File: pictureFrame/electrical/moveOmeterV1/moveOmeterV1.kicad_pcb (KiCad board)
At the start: 2 copper layers, 11 parts, among them U1 SEN0623

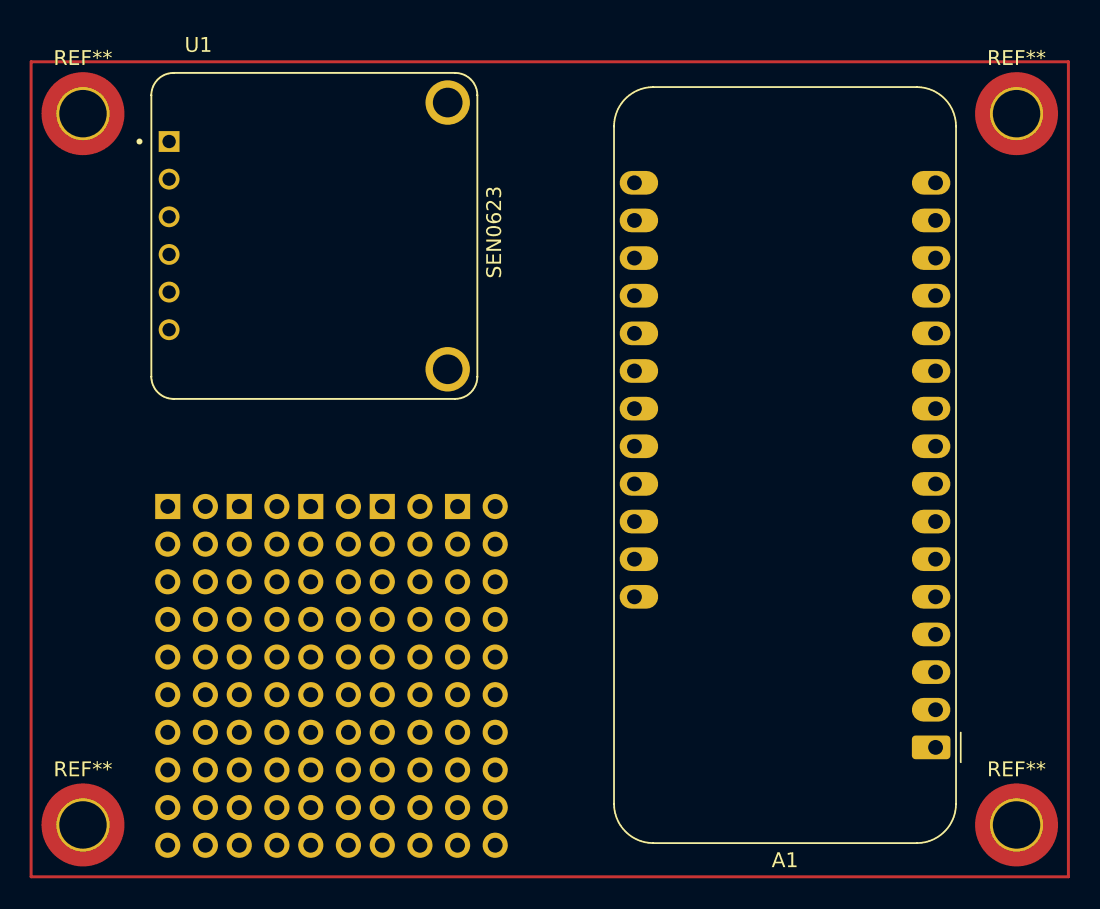
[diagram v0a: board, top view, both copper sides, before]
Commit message: Hardware: KiCad PCB v1 updates, hardware v0.01 files, new part libraries
- Update moveOmeterV1 schematic and PCB layout
- Add STEP export files (moveOmeterV1.step, moveOmeterV1_fused.step)
- Remove stale lock files and auto-saved backup files
- Add hardware version 0.01 files (2026-04-06)
- Add Adafruit ESP32-C6 and Eagle KiCad part libraries

Co-Authored-By: Claude Sonnet 4.6 <noreply@anthropic.com>
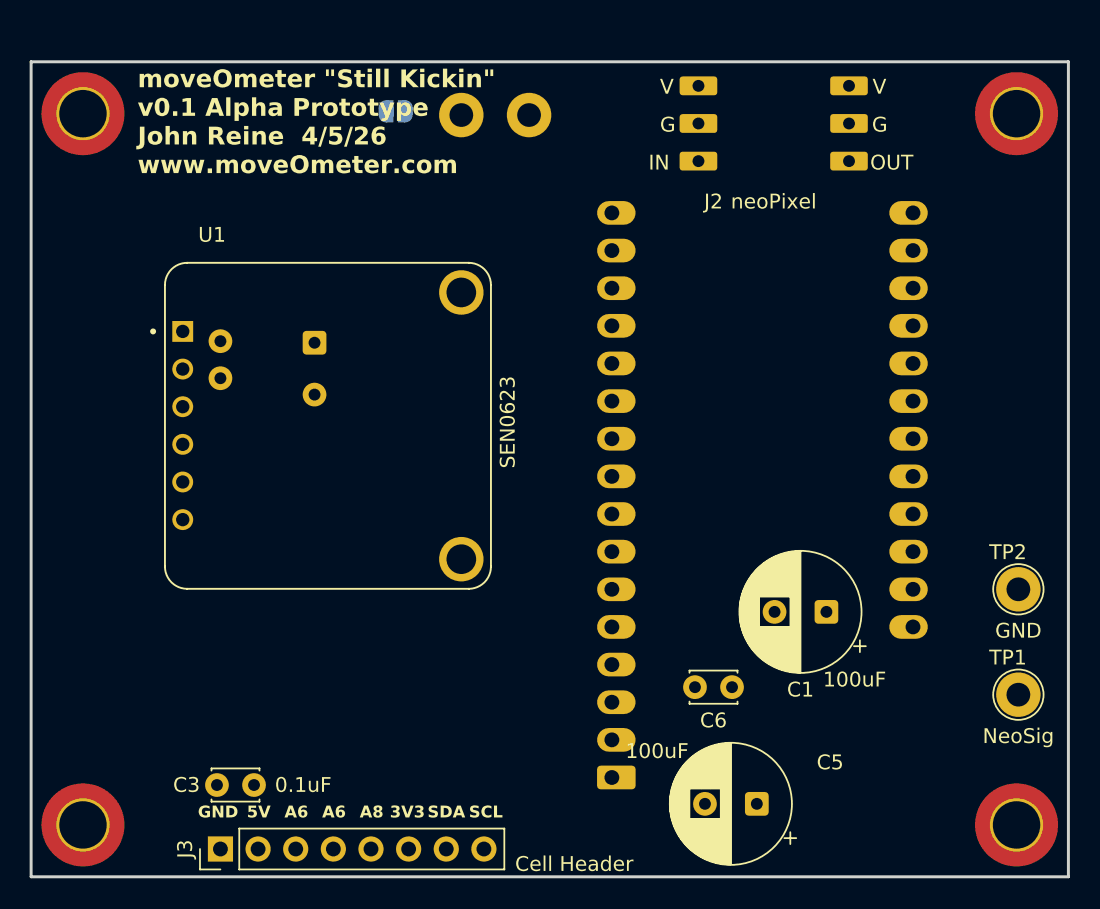
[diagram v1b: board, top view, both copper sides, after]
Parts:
- removed the REF** at (109.2, 80.0)
- removed the REF** at (123.7, 80.0)
- removed the REF** at (128.8, 80.0)
- removed the REF** at (114.0, 80.0)
- removed the REF** at (118.9, 80.0)
- added C1: 100uF, Capacitor_THT:CP_Radial_D8.0mm_P3.50mm, F.Cu at (153.7, 87.1)
- added C2: 0.1uF, Capacitor_THT:C_Disc_D3.0mm_W2.0mm_P2.50mm, B.Cu at (112.8, 68.9)
- added C3: 0.1uF, Capacitor_THT:C_Disc_D3.0mm_W2.0mm_P2.50mm, F.Cu at (115.0, 98.8)
- added C4: 100uF, Capacitor_THT:CP_Radial_D8.0mm_P3.50mm, B.Cu at (119.1, 69.0)
- added C5: 100uF, Capacitor_THT:CP_Radial_D8.0mm_P3.50mm, F.Cu at (149.0, 100.1)
- added C6: 0.1uF, Capacitor_THT:C_Disc_D3.0mm_W2.0mm_P2.50mm, F.Cu at (147.3, 92.2)
- added J2: neoPixel, Module:neoPixel6pin, F.Cu at (150.1, 46.5)
- added J3: Cell Header, Connector_PinHeader_2.54mm:PinHeader_1x08_P2.54mm_Vertical, F.Cu at (112.8, 103.1)
- added JP1: SolderJumper_2_Open, Jumper:SolderJumper-2_P1.3mm_Open_RoundedPad1.0x1.5mm, B.Cu at (124.6, 53.3)
- added TP1: NeoSig, TestPoint:TestPoint_Loop_D2.60mm_Drill1.6mm_Beaded, F.Cu at (166.6, 92.7)
- added TP2: GND, TestPoint:TestPoint_Loop_D2.60mm_Drill1.6mm_Beaded, F.Cu at (166.6, 85.6)
- added TP3: SENS_RX, TestPoint:TestPoint_Loop_D2.60mm_Drill1.6mm_Beaded, B.Cu at (129.0, 53.6)
- added TP4: SENS_TX, TestPoint:TestPoint_Loop_D2.60mm_Drill1.6mm_Beaded, B.Cu at (133.6, 53.6)
- A1: value Adafruit_Feather_HUZZAH32_ESP32 -> Adafruit_Feather_ESP32-C6; moved to B.Cu
- moved A1 21.9 mm to (139.2, 98.3), turned to 0 degrees
- moved U1 12.8 mm to (120.0, 74.6)
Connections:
- A1 pad 14: unconnected-(A1-RX/IO16-Pad14) -> /SENS_RX
- A1 pad 15: unconnected-(A1-TX/IO17-Pad15) -> /SENS_TX
- A1 pad 19: unconnected-(A1-A6/IO14-Pad19) -> /A6
- A1 pad 2: unconnected-(A1-3V3-Pad2) -> +3V3 500mA
- A1 pad 20: unconnected-(A1-A7/IO32-Pad20) -> /A7
- A1 pad 21: unconnected-(A1-A8/IO15-Pad21) -> /A8
- A1 pad 22: unconnected-(A1-A9/IO33-Pad22) -> /A9
- A1 pad 26: unconnected-(A1-USB-Pad26) -> /5V_USB
- A1 pad 4: unconnected-(A1-GND-Pad4) -> GND
- A1 pad 5: unconnected-(A1-DAC2/A0-Pad5) -> Net-(A1-DAC2/A0)
- A1 pad 6: unconnected-(A1-DAC1/A1-Pad6) -> /SCL
- A1 pad 7: unconnected-(A1-I34/A2-Pad7) -> /SDA
- A1 pad 8: unconnected-(A1-I39/A3-Pad8) -> /A3
- U1 pad 1: unconnected-(U1-VIN-Pad1) -> /5V_USB
- U1 pad 2: unconnected-(U1-GND-Pad2) -> GND
- U1 pad 3: unconnected-(U1-RX-Pad3) -> /SENS_TX
- U1 pad 4: unconnected-(U1-TX-Pad4) -> /SENS_RX
- U1 pad 5: unconnected-(U1-IO1-Pad5) -> Net-(A1-DAC2/A0)
- U1 pad 6: unconnected-(U1-IO2-Pad6) -> /A9
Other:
- board outline added: 70 x 55 mm
- board text added: "3V3"
- board text added: "5V"
- board text added: "A6"
- board text added: "A8"
- board text added: "GND"
- board text added: "SCL"
- board text added: "SDA"
- board text added: "moveOmeter {dblquote}Still Kickin{dblquote} v0.1 Alpha Prototype John Reine 4/5/26 www.moveOmeter.com"
